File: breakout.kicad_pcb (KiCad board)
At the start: 2 copper layers, 20.7 x 16.1 mm, 7 parts, among them J1 Conn_01x03, J2 Conn_01x02

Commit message: v1.0
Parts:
- added J3: Conn_01x02, Connector_PinHeader_2.54mm:PinHeader_1x02_P2.54mm_Vertical, F.Cu at (152.2, 76.3)
- J2: footprint TerminalBlock_Phoenix:TerminalBlock_Phoenix_PTSM-0,5-2-HV-2.5-SMD_1x02-1MP_P2.50mm_Vertical -> DUST:PTSM 0.5-2-HH-2.5-SMD
- moved J1 3.32 mm to (142.3, 80.3)
- moved C2 3.05 mm to (146.5, 81.3)
- moved R2 3.05 mm to (144.9, 81.3)
- moved C1 3.05 mm to (148.1, 81.3)
- moved R1 2.88 mm to (146.4, 74.0)
- moved D1 1.90 mm to (145.6, 77.3), turned to 90 degrees
- moved J2 1.00 mm to (151.6, 77.2), turned to 90 degrees
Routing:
- net Net-(C1-Pad1): track 9.22 -> 16.0 mm
- net GND: track 1.91 -> 8.13 mm
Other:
- board size 20.7 x 16.1 mm -> 15.5 x 13 mm
- board text added: "SENS"
- board text added: "Sille Van Landschoot Nico De Witte"
- board text added: "V1.0 - 2021"

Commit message: add rounded borders :)
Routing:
- net Net-(C1-Pad1): track 16.0 -> 17.3 mm
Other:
- board size 15.5 x 13 mm -> 15.9 x 13 mm
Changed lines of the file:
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@@
     )
   )
-  (gr_line (start 140.5 84) (end 140.5 71) (layer "Edge.Cuts") (width 0.1))
-  (gr_line (start 156 84) (end 140.5 84) (layer "Edge.Cuts") (width 0.1))
-  (gr_line (start 140.5 71) (end 156 71) (layer "Edge.Cuts") (width 0.1))
-  (gr_line (start 156 71) (end 156 84) (layer "Edge.Cuts") (width 0.1))
+  (gr_arc (start 154.4 73) (end 154.4 71) (angle 90) (layer "Edge.Cuts") (width 0.1))
+  (gr_line (start 140.5 82) (end 140.5 73) (layer "Edge.Cuts") (width 0.1))
+  (gr_line (start 154.4 84) (end 142.5 84) (layer "Edge.Cuts") (width 0.1))
+  (gr_line (start 142.5 71) (end 154.4 71) (layer "Edge.Cuts") (width 0.1))
+  (gr_arc (start 154.4 82) (end 156.4 82) (angle 90) (layer "Edge.Cuts") (width 0.1))
+  (gr_line (start 156.4 73) (end 156.4 82) (layer "Edge.Cuts") (width 0.1))
+  (gr_arc (start 142.5 82) (end 142.5 84) (angle 90) (layer "Edge.Cuts") (width 0.1))
+  (gr_arc (start 142.5 73) (end 140.5 73) (angle 90) (layer "Edge.Cuts") (width 0.1))
   (gr_text "V1.0 - 2021" (at 148 82.9) (layer "B.SilkS")
     (effects (font (size 0.7 0.7) (thickness 0.1)) (justify left mirror))
@@
     (effects (font (size 0.8 0.8) (thickness 0.15)) (justify mirror))
   )
-  (gr_text "DUST Pico" (at 144.9 72.2) (layer "F.SilkS")
+  (gr_text "DUST Pico" (at 145.5 72.2) (layer "F.SilkS")
     (effects (font (size 1 1) (thickness 0.25)))
   )
@@
   )
   (dimension (type aligned) (layer "User.1")
-    (pts (xy 140.5 84) (xy 156 84))
+    (pts (xy 140.5 84) (xy 156.4 84))
     (height 1.6)
-    (gr_text "15.5 mm" (at 146.1 86) (layer "User.1")
+    (gr_text "15.9 mm" (at 146.1 86) (layer "User.1")
       (effects (font (size 1 1) (thickness 0.15)))
     )
@@
     (style (thickness 0.15) (arrow_length 1.27) (text_position_mode 2) (extension_height 0.58642) (extension_offset 0.5) keep_text_aligned)
   )
-  (segment (start 147.225 74) (end 148.4 74) (width 0.25) (layer "F.Cu") (net 1))
-  (segment (start 148.7 74.3) (end 148.7 76.25) (width 0.25) (layer "F.Cu") (net 1))
-  (segment (start 146.524511 76.574511) (end 145.6 75.65) (width 0.25) (layer "F.Cu") (net 1))
-  (segment (start 148.4 74) (end 148.7 74.3) (width 0.25) (layer "F.Cu") (net 1))
+  (segment (start 145.6 75.65) (end 145.6 75.5) (width 0.25) (layer "F.Cu") (net 1))
+  (segment (start 147.225 74) (end 147.225 74.975) (width 0.25) (layer "F.Cu") (net 1))
+  (segment (start 146.575489 79.675489) (end 146.575489 76.624511) (width 0.25) (layer "F.Cu") (net 1))
+  (segment (start 148.575 76.325) (end 152.2 76.325) (width 0.25) (layer "F.Cu") (net 1))
+  (segment (start 148.3 80.825) (end 147.22548 79.75048) (width 0.25) (layer "F.Cu") (net 1))
+  (segment (start 147.225 74.975) (end 148.575 76.325) (width 0.25) (layer "F.Cu") (net 1))
   (segment (start 147.22548 79.75048) (end 146.65048 79.75048) (width 0.25) (layer "F.Cu") (net 1))
-  (segment (start 148.775 76.325) (end 152.2 76.325) (width 0.25) (layer "F.Cu") (net 1))
-  (segment (start 145.6 75.625) (end 147.225 74) (width 0.25) (layer "F.Cu") (net 1))
-  (segment (start 148.7 76.25) (end 148.775 76.325) (width 0.25) (layer "F.Cu") (net 1))
-  (segment (start 145.6 75.65) (end 145.6 75.625) (width 0.25) (layer "F.Cu") (net 1))
-  (segment (start 146.65048 79.75048) (end 146.524511 79.624511) (width 0.25) (layer "F.Cu") (net 1))
-  (segment (start 148.3 80.825) (end 147.22548 79.75048) (width 0.25) (layer "F.Cu") (net 1))
-  (segment (start 146.524511 79.624511) (end 146.524511 76.574511) (width 0.25) (layer "F.Cu") (net 1))
+  (segment (start 146.575489 76.624511) (end 146.95 76.25) (width 0.25) (layer "F.Cu") (net 1))
+  (segment (start 147.1 74) (end 147.225 74) (width 0.25) (layer "F.Cu") (net 1))
+  (segment (start 146.95 76.25) (end 148.5 76.25) (width 0.25) (layer "F.Cu") (net 1))
+  (segment (start 146.65048 79.75048) (end 146.575489 79.675489) (width 0.25) (layer "F.Cu") (net 1))
+  (segment (start 145.75 75.65) (end 146.35 76.25) (width 0.25) (layer "F.Cu") (net 1))
+  (segment (start 146.35 76.25) (end 148.5 76.25) (width 0.25) (layer "F.Cu") (net 1))
+  (segment (start 145.6 75.65) (end 145.75 75.65) (width 0.25) (layer "F.Cu") (net 1))
   (segment (start 149.2 79.45) (end 149.2 81.5) (width 0.25) (layer "F.Cu") (net 2))
   (segment (start 148.5 78.75) (end 152.085 78.75) (width 0.25) (layer "F.Cu") (net 2))
@@
   (segment (start 145.6 78.95) (end 144.9 79.65) (width 0.25) (layer "F.Cu") (net 3))
   (segment (start 144.435 77.785) (end 145.6 78.95) (width 0.25) (layer "F.Cu") (net 3))
-  (segment (start 144.4 74.1) (end 144.5 74) (width 0.25) (layer "F.Cu") (net 4))
-  (segment (start 143.445 74.1) (end 144.4 74.1) (width 0.25) (layer "F.Cu") (net 4))
-  (segment (start 142.3 75.245) (end 143.445 74.1) (width 0.25) (layer "F.Cu") (net 4))
-  (segment (start 144.5 74) (end 145.575 74) (width 0.25) (layer "F.Cu") (net 4))
+  (segment (start 142.3 75.245) (end 143.545 74) (width 0.25) (layer "F.Cu") (net 4))
+  (segment (start 143.545 74) (end 145.575 74) (width 0.25) (layer "F.Cu") (net 4))
   (zone (net 2) (net_name "GND") (layers F&B.Cu) (hatch edge 0.508)
     (connect_pads (clearance 0.508))
@@
     (polygon
       (pts
-        (xy 156 84)
+        (xy 156.4 84)
         (xy 140.5 84)
         (xy 140.5 71)
-        (xy 156 71)
+        (xy 156.4 71)
       )
     )

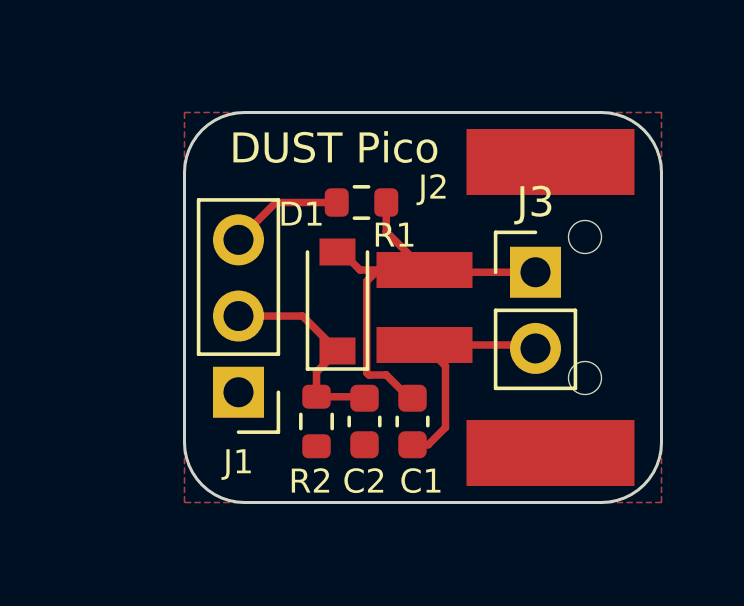
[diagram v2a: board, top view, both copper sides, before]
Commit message: add discharge circuit
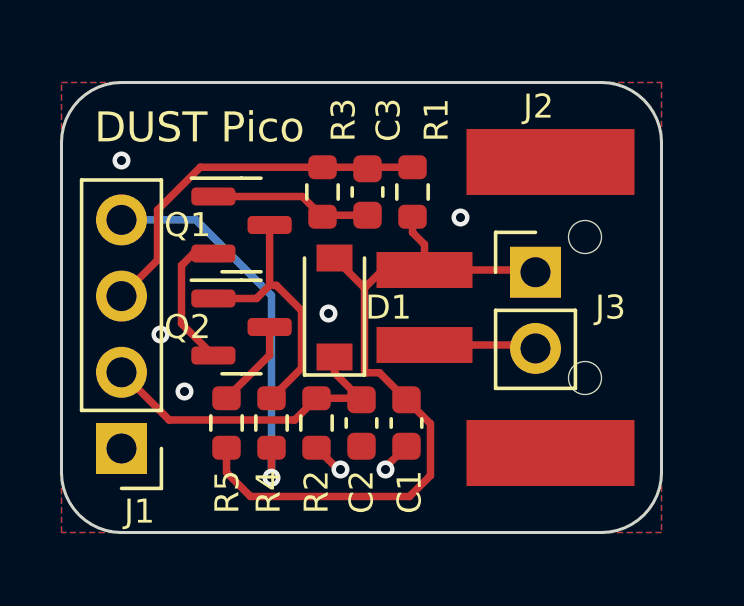
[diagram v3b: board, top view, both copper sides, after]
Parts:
- added C3: C, Capacitor_SMD:C_0603_1608Metric, F.Cu at (146.6, 73.7)
- added Q1: MMBT3904, Package_TO_SOT_SMD:SOT-23, F.Cu at (142.4, 74.8)
- added Q2: MMBT3904, Package_TO_SOT_SMD:SOT-23, F.Cu at (142.4, 78.2)
- added R3: R, Resistor_SMD:R_0603_1608Metric, F.Cu at (145.1, 73.7)
- added R4: R, Resistor_SMD:R_0603_1608Metric, F.Cu at (143.4, 81.3)
- added R5: R, Resistor_SMD:R_0603_1608Metric, F.Cu at (141.9, 81.3)
- J1: value Conn_01x03 -> Conn_01x04; footprint Connector_PinHeader_2.54mm:PinHeader_1x03_P2.54mm_Vertical -> Connector_PinHeader_2.54mm:PinHeader_1x04_P2.54mm_Vertical
- moved J1 4.33 mm to (138.4, 82.2)
- moved R1 1.74 mm to (148.1, 73.7), turned to -90 degrees
- moved D1 0.22 mm to (145.5, 77.5)
- moved C1 0.21 mm to (147.9, 81.3)
- moved C2 0.11 mm to (146.4, 81.3)
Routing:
- net /DISCHARGE: track 0.00 -> 13.1 mm, vias 0 -> 1
- net Net-(Q1-Pad3): track 0.00 -> 8.82 mm
- net /PWM: track 3.79 -> 12.5 mm
- net Net-(C1-Pad1): track 17.3 -> 25.0 mm
- net Net-(C3-Pad1): track 0.00 -> 5.44 mm
- net /OUT: track 7.05 -> 10.8 mm
- net Net-(Q2-Pad3): track 0.00 -> 2.97 mm
- net GND: track 8.13 -> 10.6 mm, vias 0 -> 7
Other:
- board size 15.9 x 13 mm -> 20 x 15 mm
- board text added: "DIS"
